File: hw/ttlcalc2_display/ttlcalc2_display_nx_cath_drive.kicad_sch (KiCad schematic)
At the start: 23 parts, among them Q16 MPSA42, Q17 MPSA42, Q18 MPSA42, Q19 MPSA42, Q20 MPSA42, Q21 MPSA42, Q22 MPSA42, Q23 MPSA42, Q24 MPSA42, Q25 MPSA42, U12 74LS04, U13 74LS42, U14 74LS04

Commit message: Continue work on display driver board schematic
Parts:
- R18: footprint Resistor_THT:R_Axial_DIN0309_L9.0mm_D3.2mm_P2.54mm_Vertical -> Resistor_THT:R_Axial_DIN0207_L6.3mm_D2.5mm_P2.54mm_Vertical
- R19: renamed from R22; footprint Resistor_THT:R_Axial_DIN0309_L9.0mm_D3.2mm_P2.54mm_Vertical -> Resistor_THT:R_Axial_DIN0207_L6.3mm_D2.5mm_P2.54mm_Vertical
- R20: renamed from R26; footprint Resistor_THT:R_Axial_DIN0309_L9.0mm_D3.2mm_P2.54mm_Vertical -> Resistor_THT:R_Axial_DIN0207_L6.3mm_D2.5mm_P2.54mm_Vertical
- R21: renamed from R19; footprint Resistor_THT:R_Axial_DIN0309_L9.0mm_D3.2mm_P2.54mm_Vertical -> Resistor_THT:R_Axial_DIN0207_L6.3mm_D2.5mm_P2.54mm_Vertical
- R22: renamed from R23; footprint Resistor_THT:R_Axial_DIN0309_L9.0mm_D3.2mm_P2.54mm_Vertical -> Resistor_THT:R_Axial_DIN0207_L6.3mm_D2.5mm_P2.54mm_Vertical
- R23: renamed from R27; footprint Resistor_THT:R_Axial_DIN0309_L9.0mm_D3.2mm_P2.54mm_Vertical -> Resistor_THT:R_Axial_DIN0207_L6.3mm_D2.5mm_P2.54mm_Vertical
- R24: renamed from R20; footprint Resistor_THT:R_Axial_DIN0309_L9.0mm_D3.2mm_P2.54mm_Vertical -> Resistor_THT:R_Axial_DIN0207_L6.3mm_D2.5mm_P2.54mm_Vertical
- R25: renamed from R24; footprint Resistor_THT:R_Axial_DIN0309_L9.0mm_D3.2mm_P2.54mm_Vertical -> Resistor_THT:R_Axial_DIN0207_L6.3mm_D2.5mm_P2.54mm_Vertical
- R26: renamed from R21; footprint Resistor_THT:R_Axial_DIN0309_L9.0mm_D3.2mm_P2.54mm_Vertical -> Resistor_THT:R_Axial_DIN0207_L6.3mm_D2.5mm_P2.54mm_Vertical
- R27: renamed from R25; footprint Resistor_THT:R_Axial_DIN0309_L9.0mm_D3.2mm_P2.54mm_Vertical -> Resistor_THT:R_Axial_DIN0207_L6.3mm_D2.5mm_P2.54mm_Vertical
- renumbered Q20 to Q17, Q24 to Q18, Q17 to Q19, Q21 to Q20, Q25 to Q21, Q18 to Q22, Q22 to Q23, Q19 to Q24, Q23 to Q25, U13 to U12, U12 to U13

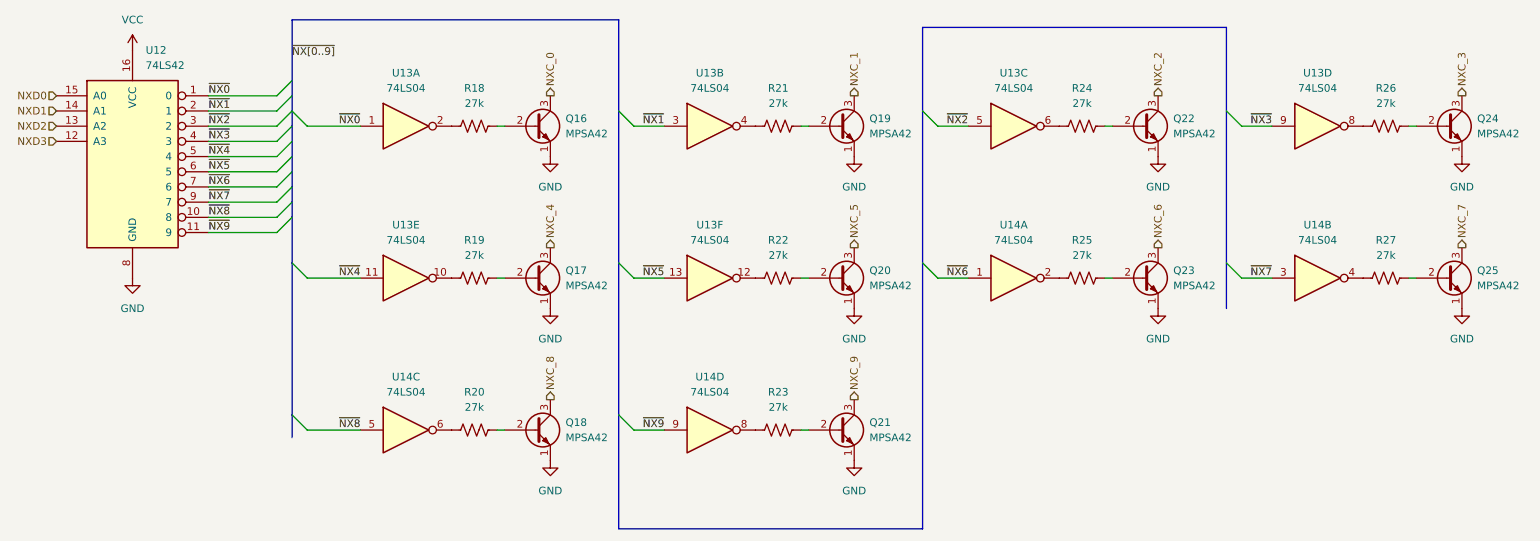
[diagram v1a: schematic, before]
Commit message: Simplify display driver board, add busy light
Removed digit storage and multiplexing logic from display driver, will handle in software instead
Add driver for busy indicator
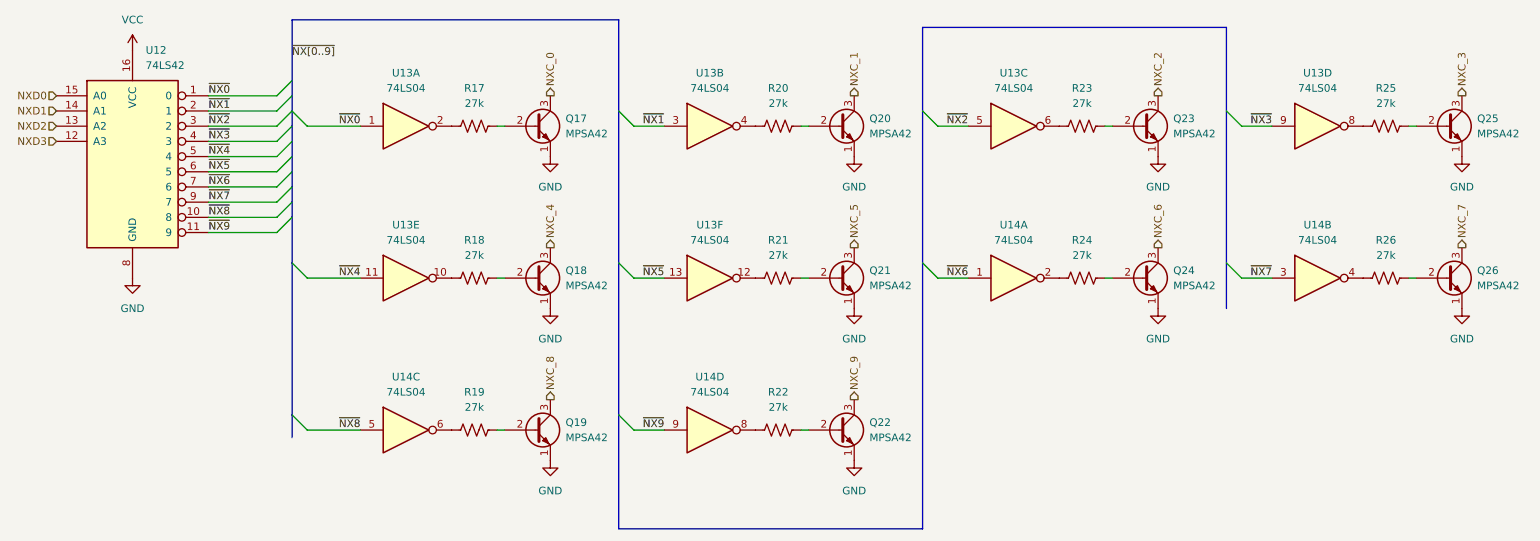
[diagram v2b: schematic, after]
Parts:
- renumbered Q16 to Q17, Q17 to Q18, Q18 to Q19, Q19 to Q20, Q20 to Q21, Q21 to Q22, Q22 to Q23, Q23 to Q24, Q24 to Q25, Q25 to Q26, R18 to R17, R19 to R18, R20 to R19, R21 to R20, R22 to R21, R23 to R22, R24 to R23, R25 to R24, R26 to R25, R27 to R26

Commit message: Display driver board routing and silkscreen tweaks
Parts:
- Q17, Q18, Q19, Q20, Q21, Q22, Q23, Q24, Q25, Q26: footprint Package_TO_SOT_THT:TO-92_Inline -> Package_TO_SOT_THT:TO-92_Inline_Wide
- R17, R18, R19, R20, R21, R22, R23, R24, R25, R26: footprint Resistor_THT:R_Axial_DIN0207_L6.3mm_D2.5mm_P2.54mm_Vertical -> Resistor_THT:R_Axial_DIN0207_L6.3mm_D2.5mm_P7.62mm_Horizontal

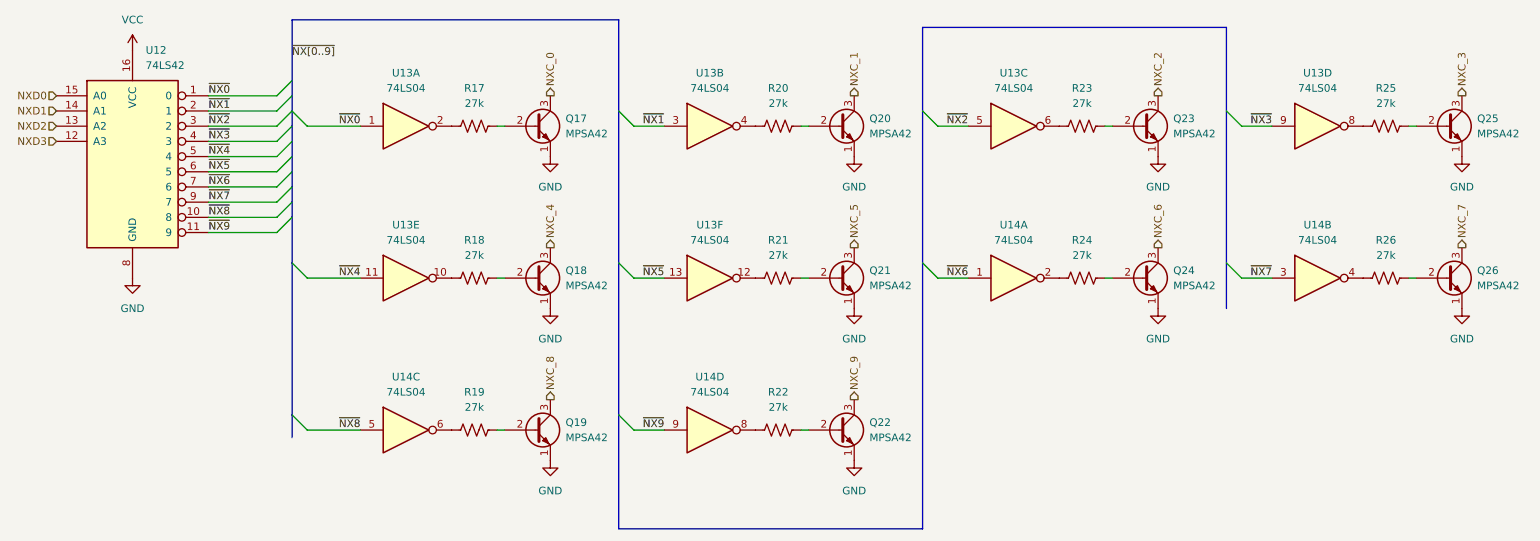
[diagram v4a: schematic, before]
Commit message: Display driver geographical reannotate
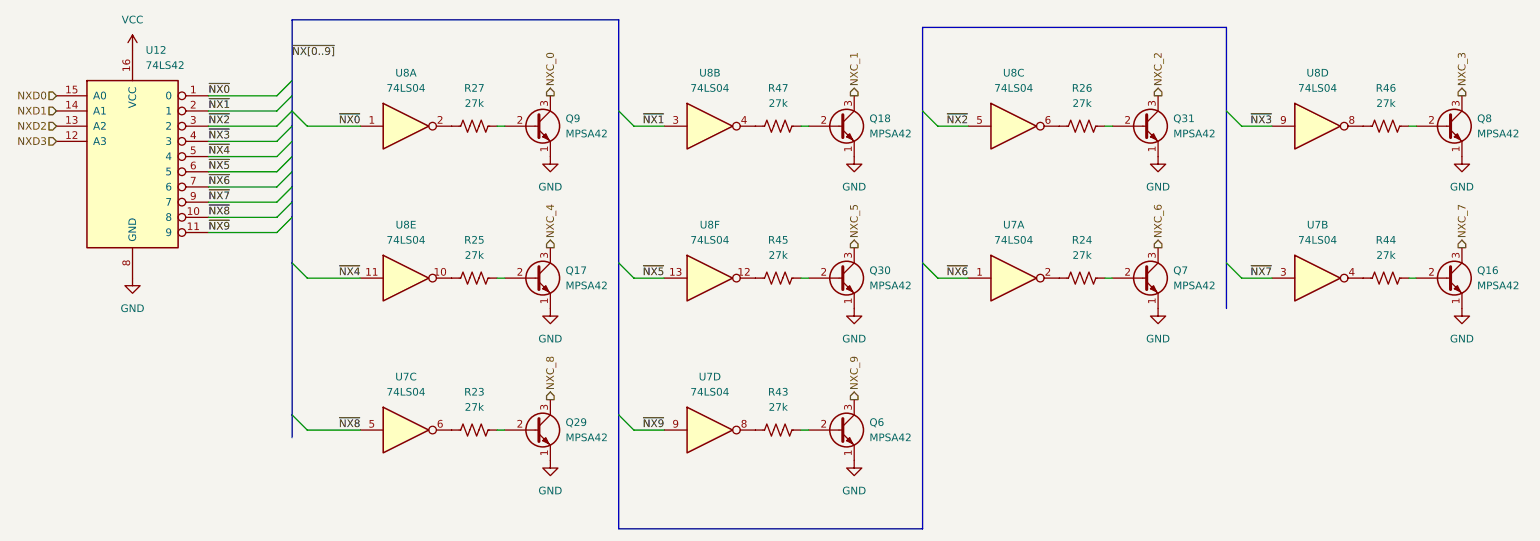
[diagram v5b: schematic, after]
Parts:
- renumbered Q26 to Q16, Q18 to Q17, Q20 to Q18, Q19 to Q29, Q21 to Q30, Q23 to Q31, Q22 to Q6, Q24 to Q7, Q25 to Q8, Q17 to Q9, R19 to R23, R18 to R25, R23 to R26, R17 to R27, R22 to R43, R26 to R44, R21 to R45, R25 to R46, R20 to R47, U14 to U7, U13 to U8
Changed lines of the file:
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@@
 		(dnp no)
 		(fields_autoplaced yes)
-		(property "Reference" "U13"
+		(property "Reference" "U8"
 			(at 78.74 57.15 0)
 			(effects
@@
 			(project "ttlcalc2_display"
 				(path "/4da693c8-a60c-4d11-a405-739e88984bfc/c57d7e5c-e6e5-4281-b6a7-42d99b39fb26"
-					(reference "U13")
+					(reference "U8")
 					(unit 5)
 				)
@@
 		(dnp no)
 		(fields_autoplaced yes)
-		(property "Reference" "R23"
+		(property "Reference" "R26"
 			(at 191.77 34.29 90)
 			(effects
@@
 			(project "ttlcalc2_display"
 				(path "/4da693c8-a60c-4d11-a405-739e88984bfc/c57d7e5c-e6e5-4281-b6a7-42d99b39fb26"
-					(reference "R23")
+					(reference "R26")
 					(unit 1)
 				)
@@
 		(dnp no)
 		(fields_autoplaced yes)
-		(property "Reference" "R18"
+		(property "Reference" "R25"
 			(at 90.17 59.69 90)
 			(effects
@@
 			(project "ttlcalc2_display"
 				(path "/4da693c8-a60c-4d11-a405-739e88984bfc/c57d7e5c-e6e5-4281-b6a7-42d99b39fb26"
-					(reference "R18")
+					(reference "R25")
 					(unit 1)
 				)
@@
 		(dnp no)
 		(fields_autoplaced yes)
-		(property "Reference" "Q22"
+		(property "Reference" "Q6"
 			(at 156.21 90.1699 0)
 			(effects
@@
 			(project "ttlcalc2_display"
 				(path "/4da693c8-a60c-4d11-a405-739e88984bfc/c57d7e5c-e6e5-4281-b6a7-42d99b39fb26"
-					(reference "Q22")
+					(reference "Q6")
 					(unit 1)
 				)
@@
 		(dnp no)
 		(fields_autoplaced yes)
-		(property "Reference" "R22"
+		(property "Reference" "R43"
 			(at 140.97 85.09 90)
 			(effects
@@
 			(project "ttlcalc2_display"
 				(path "/4da693c8-a60c-4d11-a405-739e88984bfc/c57d7e5c-e6e5-4281-b6a7-42d99b39fb26"
-					(reference "R22")
+					(reference "R43")
 					(unit 1)
 				)
@@
 		(dnp no)
 		(fields_autoplaced yes)
-		(property "Reference" "Q23"
+		(property "Reference" "Q31"
 			(at 207.01 39.3699 0)
 			(effects
@@
 			(project "ttlcalc2_display"
 				(path "/4da693c8-a60c-4d11-a405-739e88984bfc/c57d7e5c-e6e5-4281-b6a7-42d99b39fb26"
-					(reference "Q23")
+					(reference "Q31")
 					(unit 1)
 				)
@@
 		(dnp no)
 		(fields_autoplaced yes)
-		(property "Reference" "U14"
+		(property "Reference" "U7"
 			(at 180.34 57.15 0)
 			(effects
@@
 			(project "ttlcalc2_display"
 				(path "/4da693c8-a60c-4d11-a405-739e88984bfc/c57d7e5c-e6e5-4281-b6a7-42d99b39fb26"
-					(reference "U14")
+					(reference "U7")
 					(unit 1)
 				)
@@
 		(dnp no)
 		(fields_autoplaced yes)
-		(property "Reference" "Q26"
+		(property "Reference" "Q16"
 			(at 257.81 64.7699 0)
 			(effects
@@
 			(project "ttlcalc2_display"
 				(path "/4da693c8-a60c-4d11-a405-739e88984bfc/c57d7e5c-e6e5-4281-b6a7-42d99b39fb26"
-					(reference "Q26")
+					(reference "Q16")
 					(unit 1)
 				)
@@
 		(on_board yes)
 		(dnp no)
-		(property "Reference" "U13"
+		(property "Reference" "U8"
 			(at 180.34 31.75 0)
 			(effects
@@
 			(project "ttlcalc2_display"
 				(path "/4da693c8-a60c-4d11-a405-739e88984bfc/c57d7e5c-e6e5-4281-b6a7-42d99b39fb26"
-					(reference "U13")
+					(reference "U8")
 					(unit 3)
 				)
@@
 		(dnp no)
 		(fields_autoplaced yes)
-		(property "Reference" "R25"
+		(property "Reference" "R46"
 			(at 242.57 34.29 90)
 			(effects
@@
 			(project "ttlcalc2_display"
 				(path "/4da693c8-a60c-4d11-a405-739e88984bfc/c57d7e5c-e6e5-4281-b6a7-42d99b39fb26"
-					(reference "R25")
+					(reference "R46")
 					(unit 1)
 				)
@@
 		(dnp no)
 		(fields_autoplaced yes)
-		(property "Reference" "U13"
+		(property "Reference" "U8"
 			(at 78.74 31.75 0)
 			(effects
@@
 			(project "ttlcalc2_display"
 				(path "/4da693c8-a60c-4d11-a405-739e88984bfc/c57d7e5c-e6e5-4281-b6a7-42d99b39fb26"
-					(reference "U13")
+					(reference "U8")
 					(unit 1)
 				)
@@
 		(dnp no)
 		(fields_autoplaced yes)
-		(property "Reference" "U13"
+		(property "Reference" "U8"
 			(at 231.14 31.75 0)
 			(effects
@@
 			(project "ttlcalc2_display"
 				(path "/4da693c8-a60c-4d11-a405-739e88984bfc/c57d7e5c-e6e5-4281-b6a7-42d99b39fb26"
-					(reference "U13")
+					(reference "U8")
 					(unit 4)
 				)
@@
 		(dnp no)
 		(fields_autoplaced yes)
-		(property "Reference" "R17"
+		(property "Reference" "R27"
 			(at 90.17 34.29 90)
 			(effects
@@
 			(project "ttlcalc2_display"
 				(path "/4da693c8-a60c-4d11-a405-739e88984bfc/c57d7e5c-e6e5-4281-b6a7-42d99b39fb26"
-					(reference "R17")
+					(reference "R27")
 					(unit 1)
 				)
@@
 		(dnp no)
 		(fields_autoplaced yes)
-		(property "Reference" "Q17"
+		(property "Reference" "Q9"
 			(at 105.41 39.3699 0)
 			(effects
@@
 			(project "ttlcalc2_display"
 				(path "/4da693c8-a60c-4d11-a405-739e88984bfc/c57d7e5c-e6e5-4281-b6a7-42d99b39fb26"
-					(reference "Q17")
+					(reference "Q9")
 					(unit 1)
 				)
@@
 		(dnp no)
 		(fields_autoplaced yes)
-		(property "Reference" "Q18"
+		(property "Reference" "Q17"
 			(at 105.41 64.7699 0)
 			(effects
@@
 			(project "ttlcalc2_display"
 				(path "/4da693c8-a60c-4d11-a405-739e88984bfc/c57d7e5c-e6e5-4281-b6a7-42d99b39fb26"
-					(reference "Q18")
+					(reference "Q17")
 					(unit 1)
 				)
@@
 		(dnp no)
 		(fields_autoplaced yes)
-		(property "Reference" "U14"
+		(property "Reference" "U7"
 			(at 231.14 57.15 0)
 			(effects
@@
 			(project "ttlcalc2_display"
 				(path "/4da693c8-a60c-4d11-a405-739e88984bfc/c57d7e5c-e6e5-4281-b6a7-42d99b39fb26"
-					(reference "U14")
+					(reference "U7")
 					(unit 2)
 				)
@@
 		(dnp no)
 		(fields_autoplaced yes)
-		(property "Reference" "U14"
+		(property "Reference" "U7"
 			(at 78.74 82.55 0)
 			(effects
@@
 			(project "ttlcalc2_display"
 				(path "/4da693c8-a60c-4d11-a405-739e88984bfc/c57d7e5c-e6e5-4281-b6a7-42d99b39fb26"
-					(reference "U14")
+					(reference "U7")
 					(unit 3)
 				)
@@
 		(dnp no)
 		(fields_autoplaced yes)
-		(property "Reference" "U14"
+		(property "Reference" "U7"
 			(at 129.54 82.55 0)
 			(effects
@@
 			(project "ttlcalc2_display"
 				(path "/4da693c8-a60c-4d11-a405-739e88984bfc/c57d7e5c-e6e5-4281-b6a7-42d99b39fb26"
-					(reference "U14")
+					(reference "U7")
 					(unit 4)
 				)
@@
 		(dnp no)
 		(fields_autoplaced yes)
-		(property "Reference" "Q21"
+		(property "Reference" "Q30"
 			(at 156.21 64.7699 0)
 			(effects
@@
 			(project "ttlcalc2_display"
 				(path "/4da693c8-a60c-4d11-a405-739e88984bfc/c57d7e5c-e6e5-4281-b6a7-42d99b39fb26"
-					(reference "Q21")
+					(reference "Q30")
 					(unit 1)
 				)
@@
 		(dnp no)
 		(fields_autoplaced yes)
-		(property "Reference" "U13"
+		(property "Reference" "U8"
 			(at 129.54 57.15 0)
 			(effects
@@
 			(project "ttlcalc2_display"
 				(path "/4da693c8-a60c-4d11-a405-739e88984bfc/c57d7e5c-e6e5-4281-b6a7-42d99b39fb26"
-					(reference "U13")
+					(reference "U8")
 					(unit 6)
 				)
@@
 		(dnp no)
 		(fields_autoplaced yes)
-		(property "Reference" "R19"
+		(property "Reference" "R23"
 			(at 90.17 85.09 90)
 			(effects
@@
 			(project "ttlcalc2_display"
 				(path "/4da693c8-a60c-4d11-a405-739e88984bfc/c57d7e5c-e6e5-4281-b6a7-42d99b39fb26"
-					(reference "R19")
+					(reference "R23")
 					(unit 1)
 				)
@@
 		(dnp no)
 		(fields_autoplaced yes)
-		(property "Reference" "Q19"
+		(property "Reference" "Q29"
 			(at 105.41 90.1699 0)
 			(effects
@@
 			(project "ttlcalc2_display"
 				(path "/4da693c8-a60c-4d11-a405-739e88984bfc/c57d7e5c-e6e5-4281-b6a7-42d99b39fb26"
-					(reference "Q19")
+					(reference "Q29")
 					(unit 1)
 				)
@@
 		(dnp no)
 		(fields_autoplaced yes)
-		(property "Reference" "Q25"
+		(property "Reference" "Q8"
 			(at 257.81 39.3699 0)
 			(effects
@@
 			(project "ttlcalc2_display"
 				(path "/4da693c8-a60c-4d11-a405-739e88984bfc/c57d7e5c-e6e5-4281-b6a7-42d99b39fb26"
-					(reference "Q25")
+					(reference "Q8")
 					(unit 1)
 				)
@@
 		(dnp no)
 		(fields_autoplaced yes)
-		(property "Reference" "R20"
+		(property "Reference" "R47"
 			(at 140.97 34.29 90)
 			(effects
@@
 			(project "ttlcalc2_display"
 				(path "/4da693c8-a60c-4d11-a405-739e88984bfc/c57d7e5c-e6e5-4281-b6a7-42d99b39fb26"
-					(reference "R20")
+					(reference "R47")
 					(unit 1)
 				)
@@
 		(dnp no)
 		(fields_autoplaced yes)
-		(property "Reference" "Q24"
+		(property "Reference" "Q7"
 			(at 207.01 64.7699 0)
 			(effects
@@
 			(project "ttlcalc2_display"
 				(path "/4da693c8-a60c-4d11-a405-739e88984bfc/c57d7e5c-e6e5-4281-b6a7-42d99b39fb26"
-					(reference "Q24")
+					(reference "Q7")
 					(unit 1)
 				)
@@
 		(dnp no)
 		(fields_autoplaced yes)
-		(property "Reference" "R26"
+		(property "Reference" "R44"
 			(at 242.57 59.69 90)
 			(effects
@@
 			(project "ttlcalc2_display"
 				(path "/4da693c8-a60c-4d11-a405-739e88984bfc/c57d7e5c-e6e5-4281-b6a7-42d99b39fb26"
-					(reference "R26")
+					(reference "R44")
 					(unit 1)
 				)
@@
 		(dnp no)
 		(fields_autoplaced yes)
-		(property "Reference" "Q20"
+		(property "Reference" "Q18"
 			(at 156.21 39.3699 0)
 			(effects
@@
 			(project "ttlcalc2_display"
 				(path "/4da693c8-a60c-4d11-a405-739e88984bfc/c57d7e5c-e6e5-4281-b6a7-42d99b39fb26"
-					(reference "Q20")
+					(reference "Q18")
 					(unit 1)
 				)
@@
 		(dnp no)
 		(fields_autoplaced yes)
-		(property "Reference" "R21"
+		(property "Reference" "R45"
 			(at 140.97 59.69 90)
 			(effects
@@
 			(project "ttlcalc2_display"
 				(path "/4da693c8-a60c-4d11-a405-739e88984bfc/c57d7e5c-e6e5-4281-b6a7-42d99b39fb26"
-					(reference "R21")
+					(reference "R45")
 					(unit 1)
 				)
@@
 		(on_board yes)
 		(dnp no)
-		(property "Reference" "U13"
+		(property "Reference" "U8"
 			(at 129.54 31.75 0)
 			(effects
@@
 			(project "ttlcalc2_display"
 				(path "/4da693c8-a60c-4d11-a405-739e88984bfc/c57d7e5c-e6e5-4281-b6a7-42d99b39fb26"
-					(reference "U13")
+					(reference "U8")
 					(unit 2)
 				)
